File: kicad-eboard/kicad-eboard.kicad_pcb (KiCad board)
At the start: 2 copper layers, 92 parts, among them J1 Conn_01x02, J19 Conn_01x10, SW10 AMT10_Encoder, SW4 LIMIT_1, SW5 LIMIT_2, SW6 AMT10_Encoder, SW7 AMT10_Encoder, SW8 AMT10_Encoder, SW9 AMT10_Encoder, U1 TinkerBoard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

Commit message: Add autograph B-)
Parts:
- moved G1 2.50 mm to (54.8, 38.8)
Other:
- board text added: "Gabriel Krell 2019"
- board text added: "IIT RMC Season 4"
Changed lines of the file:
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@@
   (general
     (thickness 1.6)
-    (drawings 3)
+    (drawings 5)
     (tracks 673)
     (zones 0)
@@
   )
   (module Symbol:KiCad-Logo2_8mm_SilkScreen (layer F.Cu)
-    (at 54.75 36.25)
+    (at 54.75 38.75)
     (descr "KiCad Logo")
     (tags "Logo KiCad")
@@
     )
   )
+  (gr_text "Gabriel Krell 2019" (at 55 31.25) (layer F.SilkS)
+    (effects (font (size 1.5 1.5) (thickness 0.3)))
+  )
+  (gr_text "IIT RMC Season 4" (at 55.25 76) (layer F.SilkS)
+    (effects (font (size 1.5 1.5) (thickness 0.3)))
+  )
   (gr_line (start 41.75 97.25) (end 68.25 97.25) (layer F.SilkS) (width 0.15))
   (gr_line (start 68.25 82) (end 68.25 97.25) (layer F.SilkS) (width 0.15))
@@
   (segment (start 51.2496 89.5) (end 51.75 88.9996) (width 0.25) (layer F.Cu) (net 5))
   (segment (start 47.75 89.5) (end 51.2496 89.5) (width 0.25) (layer F.Cu) (net 5))
-  (segment (start 45 60.27587) (end 45 70.5) (width 0.25) (layer B.Cu) (net 5))
-  (segment (start 33.97553 49.2514) (end 45 60.27587) (width 0.25) (layer B.Cu) (net 5))
+  (via (at 43 70.5) (size 0.8) (drill 0.4) (layers F.Cu B.Cu) (net 5))
   (segment (start 30.865001 47.900001) (end 32.2164 49.2514) (width 0.25) (layer B.Cu) (net 5))
+  (segment (start 43 69.934315) (end 43 70.5) (width 0.25) (layer B.Cu) (net 5))
+  (segment (start 43 58.27587) (end 43 69.934315) (width 0.25) (layer B.Cu) (net 5))
+  (segment (start 33.97553 49.2514) (end 43 58.27587) (width 0.25) (layer B.Cu) (net 5))
   (segment (start 32.2164 49.2514) (end 33.97553 49.2514) (width 0.25) (layer B.Cu) (net 5))
-  (via (at 45 71) (size 0.8) (drill 0.4) (layers F.Cu B.Cu) (net 5))
-  (segment (start 45 70.5) (end 45 71) (width 0.25) (layer B.Cu) (net 5))
-  (via (at 45 73) (size 0.8) (drill 0.4) (layers F.Cu B.Cu) (net 5))
-  (segment (start 45 71) (end 45 73) (width 0.25) (layer F.Cu) (net 5))
-  (segment (start 45 75.09) (end 53.66 83.75) (width 0.25) (layer B.Cu) (net 5))
-  (segment (start 45 73) (end 45 75.09) (width 0.25) (layer B.Cu) (net 5))
+  (via (at 43 72.75) (size 0.8) (drill 0.4) (layers F.Cu B.Cu) (net 5))
+  (segment (start 43 73.09) (end 43 72.75) (width 0.25) (layer B.Cu) (net 5))
+  (segment (start 53.66 83.75) (end 43 73.09) (width 0.25) (layer B.Cu) (net 5))
+  (segment (start 43 70.5) (end 43 72.75) (width 0.25) (layer F.Cu) (net 5))
   (segment (start 52.6375 17.75) (end 56.25 21.3625) (width 1) (layer F.Cu) (net 6))
   (segment (start 46.25 17.75) (end 52.6375 17.75) (width 1) (layer F.Cu) (net 6))

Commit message: Add version number silkscreen
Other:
- board text added: "v1"
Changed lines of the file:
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@@
   (general
     (thickness 1.6)
-    (drawings 5)
+    (drawings 6)
     (tracks 673)
     (zones 0)
@@
     )
   )
+  (gr_text v1 (at 74.75 102.25) (layer F.SilkS)
+    (effects (font (size 1.5 1.5) (thickness 0.3)))
+  )
   (gr_text "Gabriel Krell 2019" (at 55 31.25) (layer F.SilkS)

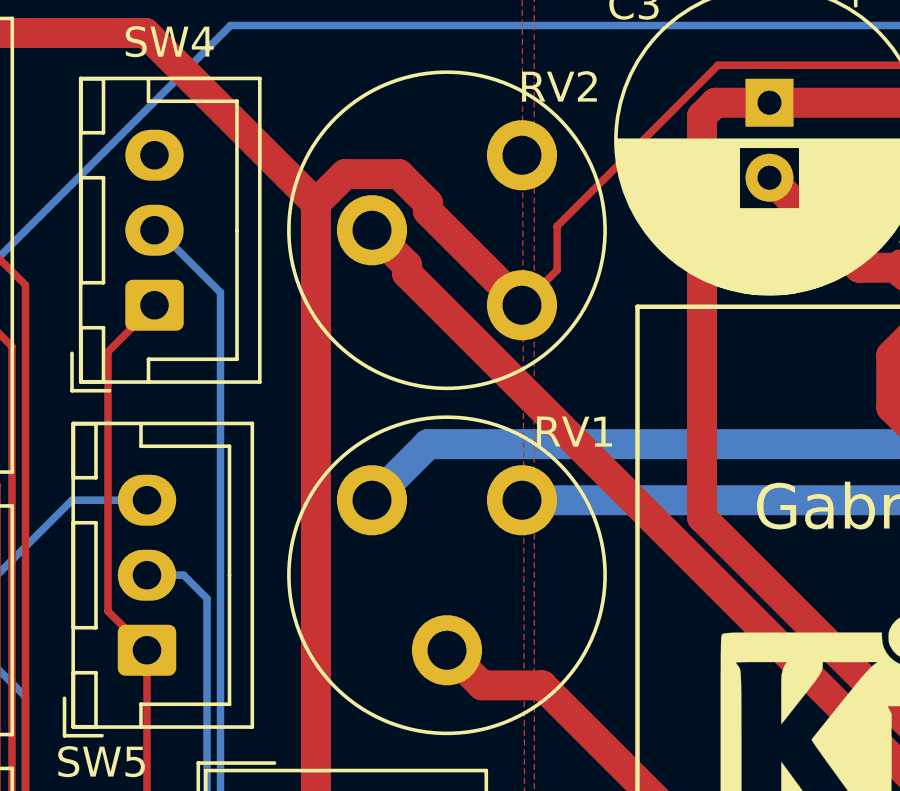
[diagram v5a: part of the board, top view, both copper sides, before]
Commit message: Add orientation symbol to pots
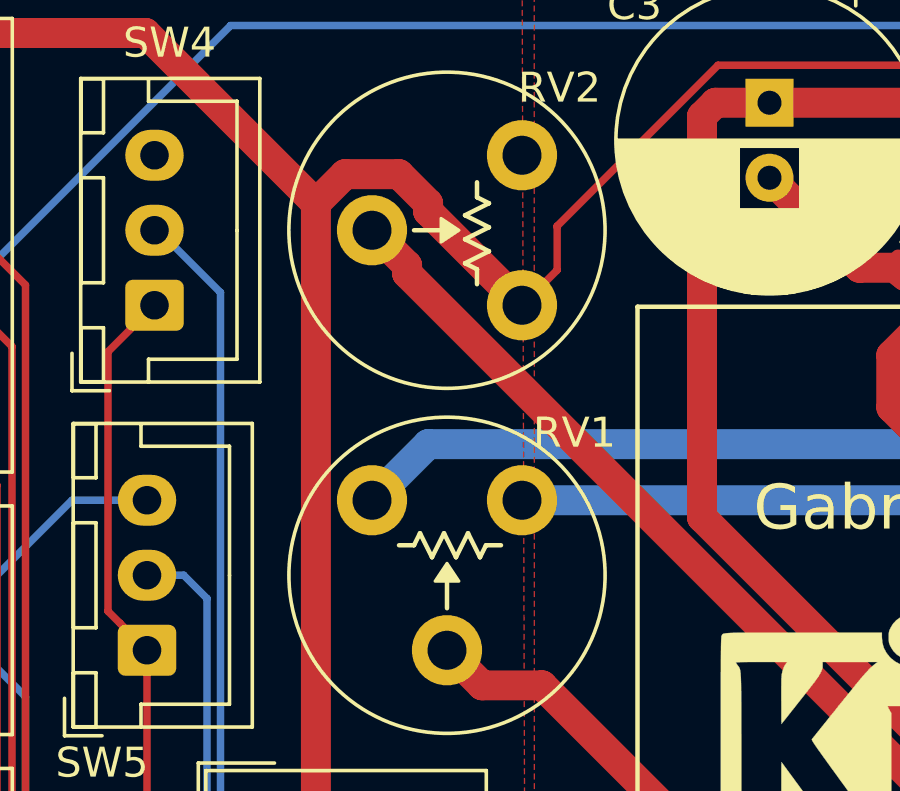
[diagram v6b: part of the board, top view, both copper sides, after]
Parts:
- RV1, RV2: footprint Potentiometer_THT:Potentiometer_Piher_PT-10-V05_Vertical -> 2019Spacehawks:Potentiometer_Piher_PT-10-V05_Vertical_SS
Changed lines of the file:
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@@
     (add_net "Net-(TP3-Pad1)")
+  )
+  (module 2019Spacehawks:Potentiometer_Piher_PT-10-V05_Vertical_SS (layer F.Cu)
+    (at 38 19.5 180)
+    (descr "Potentiometer, vertical, Piher PT-10-V05, http://www.piher-nacesa.com/pdf/12-PT10v03.pdf")
+    (tags "Potentiometer vertical Piher PT-10-V05")
+    (fp_text reference RV2 (at -1.25 2.25 180) (layer F.SilkS)
+      (effects (font (size 1 1) (thickness 0.15)))
+    )
+    (fp_text value 10K (at 2.5 3.9 180) (layer F.Fab)
+      (effects (font (size 1 1) (thickness 0.15)))
+    )
+    (fp_line (start 1.5 -4.3) (end 1.5 -3.8) (layer F.SilkS) (width 0.15))
+    (fp_line (start 1.1 -3.2) (end 1.9 -2.8) (layer F.SilkS) (width 0.15))
+    (fp_line (start 1.1 -2.4) (end 1.9 -2) (layer F.SilkS) (width 0.15))
+    (fp_line (start 1.9 -3.6) (end 1.1 -3.2) (layer F.SilkS) (width 0.15))
+    (fp_line (start 1.9 -2.8) (end 1.1 -2.4) (layer F.SilkS) (width 0.15))
+    (fp_line (start 1.1 -1.6) (end 1.5 -1.4) (layer F.SilkS) (width 0.15))
+    (fp_line (start 1.9 -2) (end 1.1 -1.6) (layer F.SilkS) (width 0.15))
+    (fp_line (start 1.5 -1.4) (end 1.5 -0.9) (layer F.SilkS) (width 0.15))
+    (fp_line (start 1.5 -3.8) (end 1.9 -3.6) (layer F.SilkS) (width 0.15))
+    (fp_line (start 2.7 -2.5) (end 3.6 -2.5) (layer F.SilkS) (width 0.15))
+    (fp_poly (pts (xy 2.1 -2.5) (xy 2.7 -2.9) (xy 2.7 -2.1)) (layer F.SilkS) (width 0.1))
+    (fp_text user %R (at -1.45 -2.5 270) (layer F.Fab)
+      (effects (font (size 1 1) (thickness 0.15)))
+    )
+    (fp_line (start 7.9 -7.9) (end -2.9 -7.9) (layer F.CrtYd) (width 0.05))
+    (fp_line (start 7.9 2.95) (end 7.9 -7.9) (layer F.CrtYd) (width 0.05))
+    (fp_line (start -2.9 2.95) (end 7.9 2.95) (layer F.CrtYd) (width 0.05))
+    (fp_line (start -2.9 -7.9) (end -2.9 2.95) (layer F.CrtYd) (width 0.05))
+    (fp_circle (center 2.501 -2.5) (end 7.771 -2.5) (layer F.SilkS) (width 0.12))
+    (fp_circle (center 2.5 -2.5) (end 4 -2.5) (layer F.Fab) (width 0.1))
+    (fp_circle (center 2.5 -2.5) (end 7.65 -2.5) (layer F.Fab) (width 0.1))
+    (pad 1 thru_hole circle (at 0 0 180) (size 2.34 2.34) (drill 1.3) (layers *.Cu *.Mask)
+      (net 7 GND))
+    (pad 2 thru_hole circle (at 5 -2.5 180) (size 2.34 2.34) (drill 1.3) (layers *.Cu *.Mask)
+      (net 49 "Net-(RV2-Pad2)"))
+    (pad 3 thru_hole circle (at 0 -5 180) (size 2.34 2.34) (drill 1.3) (layers *.Cu *.Mask)
+      (net 10 +5V))
+    (model ${KISYS3DMOD}/Potentiometer_THT.3dshapes/Potentiometer_Piher_PT-10-V05_Vertical.wrl
+      (at (xyz 0 0 0))
+      (scale (xyz 1 1 1))
+      (rotate (xyz 0 0 0))
+    )
+  )
+  (module 2019Spacehawks:Potentiometer_Piher_PT-10-V05_Vertical_SS (layer F.Cu)
+    (at 33 31 270)
+    (descr "Potentiometer, vertical, Piher PT-10-V05, http://www.piher-nacesa.com/pdf/12-PT10v03.pdf")
+    (tags "Potentiometer vertical Piher PT-10-V05")
+    (fp_text reference RV1 (at -2.25 -6.75) (layer F.SilkS)
+      (effects (font (size 1 1) (thickness 0.15)))
+    )
+    (fp_text value 10K (at 2.5 3.9 270) (layer F.Fab)
+      (effects (font (size 1 1) (thickness 0.15)))
+    )
+    (fp_line (start 1.5 -4.3) (end 1.5 -3.8) (layer F.SilkS) (width 0.15))
+    (fp_line (start 1.1 -3.2) (end 1.9 -2.8) (layer F.SilkS) (width 0.15))
+    (fp_line (start 1.1 -2.4) (end 1.9 -2) (layer F.SilkS) (width 0.15))
+    (fp_line (start 1.9 -3.6) (end 1.1 -3.2) (layer F.SilkS) (width 0.15))
+    (fp_line (start 1.9 -2.8) (end 1.1 -2.4) (layer F.SilkS) (width 0.15))
+    (fp_line (start 1.1 -1.6) (end 1.5 -1.4) (layer F.SilkS) (width 0.15))
+    (fp_line (start 1.9 -2) (end 1.1 -1.6) (layer F.SilkS) (width 0.15))
+    (fp_line (start 1.5 -1.4) (end 1.5 -0.9) (layer F.SilkS) (width 0.15))
+    (fp_line (start 1.5 -3.8) (end 1.9 -3.6) (layer F.SilkS) (width 0.15))
+    (fp_line (start 2.7 -2.5) (end 3.6 -2.5) (layer F.SilkS) (width 0.15))
+    (fp_poly (pts (xy 2.1 -2.5) (xy 2.7 -2.9) (xy 2.7 -2.1)) (layer F.SilkS) (width 0.1))
+    (fp_text user %R (at -1.45 -2.5 180) (layer F.Fab)
+      (effects (font (size 1 1) (thickness 0.15)))
+    )
+    (fp_line (start 7.9 -7.9) (end -2.9 -7.9) (layer F.CrtYd) (width 0.05))
+    (fp_line (start 7.9 2.95) (end 7.9 -7.9) (layer F.CrtYd) (width 0.05))
+    (fp_line (start -2.9 2.95) (end 7.9 2.95) (layer F.CrtYd) (width 0.05))
+    (fp_line (start -2.9 -7.9) (end -2.9 2.95) (layer F.CrtYd) (width 0.05))
+    (fp_circle (center 2.501 -2.5) (end 7.771 -2.5) (layer F.SilkS) (width 0.12))
+    (fp_circle (center 2.5 -2.5) (end 4 -2.5) (layer F.Fab) (width 0.1))
+    (fp_circle (center 2.5 -2.5) (end 7.65 -2.5) (layer F.Fab) (width 0.1))
+    (pad 1 thru_hole circle (at 0 0 270) (size 2.34 2.34) (drill 1.3) (layers *.Cu *.Mask)
+      (net 8 GNDA))
+    (pad 2 thru_hole circle (at 5 -2.5 270) (size 2.34 2.34) (drill 1.3) (layers *.Cu *.Mask)
+      (net 50 "Net-(RV1-Pad2)"))
+    (pad 3 thru_hole circle (at 0 -5 270) (size 2.34 2.34) (drill 1.3) (layers *.Cu *.Mask)
+      (net 1 +12V))
+    (model ${KISYS3DMOD}/Potentiometer_THT.3dshapes/Potentiometer_Piher_PT-10-V05_Vertical.wrl
+      (at (xyz 0 0 0))
+      (scale (xyz 1 1 1))
+      (rotate (xyz 0 0 0))
+    )
   )
   (module 2019Spacehawks:SSH_logo (layer F.Cu)
@@
     )
   )
-  (module Potentiometer_THT:Potentiometer_Piher_PT-10-V05_Vertical (layer F.Cu)
-    (at 38 19.5 180)
-    (descr "Potentiometer, vertical, Piher PT-10-V05, http://www.piher-nacesa.com/pdf/12-PT10v03.pdf")
-    (tags "Potentiometer vertical Piher PT-10-V05")
-    (fp_text reference RV2 (at -1.25 2.25 180) (layer F.SilkS)
-      (effects (font (size 1 1) (thickness 0.15)))
-    )
-    (fp_text value 10K (at 2.5 3.9 180) (layer F.Fab)
-      (effects (font (size 1 1) (thickness 0.15)))
-    )
-    (fp_text user %R (at -1.45 -2.5 270) (layer F.Fab)
-      (effects (font (size 1 1) (thickness 0.15)))
-    )
-    (fp_line (start 7.9 -7.9) (end -2.9 -7.9) (layer F.CrtYd) (width 0.05))
-    (fp_line (start 7.9 2.95) (end 7.9 -7.9) (layer F.CrtYd) (width 0.05))
-    (fp_line (start -2.9 2.95) (end 7.9 2.95) (layer F.CrtYd) (width 0.05))
-    (fp_line (start -2.9 -7.9) (end -2.9 2.95) (layer F.CrtYd) (width 0.05))
-    (fp_circle (center 2.501 -2.5) (end 7.771 -2.5) (layer F.SilkS) (width 0.12))
-    (fp_circle (center 2.5 -2.5) (end 4 -2.5) (layer F.Fab) (width 0.1))
-    (fp_circle (center 2.5 -2.5) (end 7.65 -2.5) (layer F.Fab) (width 0.1))
-    (pad 1 thru_hole circle (at 0 0 180) (size 2.34 2.34) (drill 1.3) (layers *.Cu *.Mask)
-      (net 7 GND))
-    (pad 2 thru_hole circle (at 5 -2.5 180) (size 2.34 2.34) (drill 1.3) (layers *.Cu *.Mask)
-      (net 49 "Net-(RV2-Pad2)"))
-    (pad 3 thru_hole circle (at 0 -5 180) (size 2.34 2.34) (drill 1.3) (layers *.Cu *.Mask)
-      (net 10 +5V))
-    (model ${KISYS3DMOD}/Potentiometer_THT.3dshapes/Potentiometer_Piher_PT-10-V05_Vertical.wrl
-      (at (xyz 0 0 0))
-      (scale (xyz 1 1 1))
-      (rotate (xyz 0 0 0))
-    )
-  )
   (module TestPoint:TestPoint_Bridge_Pitch2.54mm_Drill1.0mm (layer F.Cu)
     (at 73.79 30.5 180)
@@
       (at (xyz 0 0 0))
       (scale (xyz 1 1 1))
-      (rotate (xyz 0 0 0))
-    )
-  )
-  (module Potentiometer_THT:Potentiometer_Piher_PT-10-V05_Vertical (layer F.Cu)
-    (at 33 31 270)
-    (descr "Potentiometer, vertical, Piher PT-10-V05, http://www.piher-nacesa.com/pdf/12-PT10v03.pdf")
-    (tags "Potentiometer vertical Piher PT-10-V05")
-    (fp_text reference RV1 (at -2.25 -6.75) (layer F.SilkS)
-      (effects (font (size 1 1) (thickness 0.15)))
-    )
-    (fp_text value 10K (at 2.5 3.9 270) (layer F.Fab)
-      (effects (font (size 1 1) (thickness 0.15)))
-    )
-    (fp_circle (center 2.5 -2.5) (end 7.65 -2.5) (layer F.Fab) (width 0.1))
-    (fp_circle (center 2.5 -2.5) (end 4 -2.5) (layer F.Fab) (width 0.1))
-    (fp_circle (center 2.501 -2.5) (end 7.771 -2.5) (layer F.SilkS) (width 0.12))
-    (fp_line (start -2.9 -7.9) (end -2.9 2.95) (layer F.CrtYd) (width 0.05))
-    (fp_line (start -2.9 2.95) (end 7.9 2.95) (layer F.CrtYd) (width 0.05))
-    (fp_line (start 7.9 2.95) (end 7.9 -7.9) (layer F.CrtYd) (width 0.05))
-    (fp_line (start 7.9 -7.9) (end -2.9 -7.9) (layer F.CrtYd) (width 0.05))
-    (fp_text user %R (at -1.45 -2.5 180) (layer F.Fab)
-      (effects (font (size 1 1) (thickness 0.15)))
-    )
-    (pad 3 thru_hole circle (at 0 -5 270) (size 2.34 2.34) (drill 1.3) (layers *.Cu *.Mask)
-      (net 1 +12V))
-    (pad 2 thru_hole circle (at 5 -2.5 270) (size 2.34 2.34) (drill 1.3) (layers *.Cu *.Mask)
-      (net 50 "Net-(RV1-Pad2)"))
-    (pad 1 thru_hole circle (at 0 0 270) (size 2.34 2.34) (drill 1.3) (layers *.Cu *.Mask)
-      (net 8 GNDA))
-    (model ${KISYS3DMOD}/Potentiometer_THT.3dshapes/Potentiometer_Piher_PT-10-V05_Vertical.wrl
-      (at (xyz 0 0 0))
-      (scale (xyz 1 1 1))
